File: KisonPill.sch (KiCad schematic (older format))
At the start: 39 parts, among them J1 USB_C_Receptacle_USB2.0, J2 Conn_01x19_Male, J3 Conn_01x19_Male, Q1 2N3904S-RTK/PS, Q2 2N3904S-RTK/PS, SW1 SW_Push, SW2 SW_Push, U1 CP2102N-A01-GQFN28, U2 ESP32-WROOM-32D, U3 SPX1117M3-L-3-3/TR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

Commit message: V2
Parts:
- U4: footprint KisonCommon:jtag1.27-12 -> KisonCommon:jtag1.27-10
- U7: footprint Connector_Molex:Molex_CLIK-Mate_502382-1270_1x12-1MP_P1.25mm_Vertical -> Connector_Molex:Molex_CLIK-Mate_502382-1070_1x10-1MP_P1.25mm_Vertical
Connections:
- net labels added: CP2102RX, CP2102TX, ESPRX, ESPTX
- net labels removed: RXD, RXD0, TXD, TXD0
- wire segments 56 -> 52
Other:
- moved on the sheet: R14, R15, R2, R3
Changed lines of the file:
@@
 P 1100 950
 F 0 "C1" H 1215 996 50  0000 L CNN
-F 1 "4.7uf/6.3v" H 1215 905 50  0000 L CNN
+F 1 "4.7uf/6.3v" H 650 850 50  0000 L CNN
 F 2 "Capacitor_SMD:C_0603_1608Metric" H 1138 800 50  0001 C CNN
 F 3 "~" H 1100 950 50  0001 C CNN
@@
 	1800 1200 1900 1200
 Connection ~ 1800 1200
-Text Label 1250 3000 0    50   ~ 0
-TXD0
-Text Label 1250 3150 0    50   ~ 0
-RXD0
-$Comp
-L Device:R R2
-U 1 1 6052F69F
-P 1000 3150
-F 0 "R2" V 1000 3150 50  0000 C CNN
-F 1 "0" V 884 3150 50  0000 C CNN
-F 2 "Resistor_SMD:R_0603_1608Metric" V 930 3150 50  0001 C CNN
-F 3 "~" H 1000 3150 50  0001 C CNN
-F 4 "C429667" H 1000 3150 50  0001 C CNN "LCSC"
-	1    1000 3150
-	0    -1   -1   0
-$EndComp
 $Comp
 L Device:R R3
 U 1 1 6052FB68
-P 1000 3000
-F 0 "R3" V 1000 3000 50  0000 C CNN
-F 1 "0" V 900 3000 50  0000 C CNN
-F 2 "Resistor_SMD:R_0603_1608Metric" V 930 3000 50  0001 C CNN
-F 3 "~" H 1000 3000 50  0001 C CNN
-F 4 "C429667" H 1000 3000 50  0001 C CNN "LCSC"
-	1    1000 3000
+P 1070 2990
+F 0 "R3" V 1070 2990 50  0000 C CNN
+F 1 "0" V 970 2990 50  0000 C CNN
+F 2 "Resistor_SMD:R_0603_1608Metric" V 1000 2990 50  0001 C CNN
+F 3 "~" H 1070 2990 50  0001 C CNN
+F 4 "C429667" H 1070 2990 50  0001 C CNN "LCSC"
+	1    1070 2990
 	0    1    1    0
 $EndComp
-Text Label 750  3150 2    50   ~ 0
-TXD
-Text Label 750  3000 2    50   ~ 0
-RXD
-Wire Wire Line
-	1250 3150 1150 3150
-Wire Wire Line
-	1250 3000 1150 3000
-Wire Wire Line
-	850  3150 750  3150
-Wire Wire Line
-	850  3000 750  3000
 $Comp
 L power:GND #PWR0107
@@
 	0    -1   -1   0
 $EndComp
-Text Label 2700 1700 0    50   ~ 0
-TXD
-Text Label 2700 1600 0    50   ~ 0
-RXD
 Wire Wire Line
 	2400 1600 2700 1600
@@
 Text Label 8050 1500 2    50   ~ 0
 EN
-Text Label 9250 1800 0    50   ~ 0
-RXD0
-Text Label 9250 1600 0    50   ~ 0
-TXD0
 Text Label 5760 910  0    50   ~ 0
 EN
-Text Label 5760 980  0    50   ~ 0
+Text Label 5760 1000 0    50   ~ 0
 IO12
-Text Label 5760 1050 0    50   ~ 0
-IO14
 $Comp
 L Regulator_Linear:AZ1117-3.3 U3
@@
 Text Label 6730 3810 0    50   ~ 0
 IO22
-Text Label 6730 3910 0    50   ~ 0
-TXD0
-Text Label 6730 4010 0    50   ~ 0
-RXD0
 Text Label 6730 4110 0    50   ~ 0
 IO21
@@
 $EndComp
 $Comp
-L power:+3V3 #PWR0124
-U 1 1 6059C21E
-P 6040 1120
-F 0 "#PWR0124" H 6040 970 50  0001 C CNN
-F 1 "+3V3" H 6055 1293 50  0000 C CNN
-F 2 "" H 6040 1120 50  0001 C CNN
-F 3 "" H 6040 1120 50  0001 C CNN
-	1    6040 1120
-	1    0    0    -1
-$EndComp
-Wire Wire Line
-	6040 1120 5760 1120
-$Comp
-L Device:R R15
-U 1 1 605D512D
-P 6320 1190
-F 0 "R15" V 6320 1190 50  0000 C CNN
-F 1 "0" V 6400 1190 50  0000 C CNN
-F 2 "Resistor_SMD:R_0603_1608Metric" V 6250 1190 50  0001 C CNN
-F 3 "~" H 6320 1190 50  0001 C CNN
-	1    6320 1190
-	0    1    1    0
-$EndComp
-Text Label 6470 1190 0    50   ~ 0
-TXD0
-$Comp
 L KisonCommon:ESP32FullConnector U7
 U 1 1 605F623D
@@
 F 0 "U7" H 5560 2304 50  0000 C CNN
 F 1 "ESP32FullConnector" H 5560 2213 50  0000 C CNN
-F 2 "Connector_Molex:Molex_CLIK-Mate_502382-1270_1x12-1MP_P1.25mm_Vertical" H 5750 1880 50  0001 C CNN
+F 2 "Connector_Molex:Molex_CLIK-Mate_502382-1070_1x10-1MP_P1.25mm_Vertical" H 5750 1880 50  0001 C CNN
 F 3 "" H 5750 1880 50  0001 C CNN
 	1    5750 1880
@@
 	-1   0    0    1
 $EndComp
-Text Label 5340 980  2    50   ~ 0
+Text Label 5340 1000 2    50   ~ 0
 IO13
-Text Label 5340 1050 2    50   ~ 0
+Text Label 5340 1090 2    50   ~ 0
 IO15
 Wire Wire Line
 	5120 910  5340 910
-Text Label 5340 1260 3    50   ~ 0
+Text Label 5340 1180 2    50   ~ 0
 IO0
-Text Label 4740 1190 2    50   ~ 0
-RXD0
 $Comp
 L KisonCommon:ESP32FullConnector U4
@@
 F 0 "U4" H 5550 1544 50  0000 C CNN
 F 1 "ESP32FullConnector-KisonCommon" H 5550 1453 50  0000 C CNN
-F 2 "KisonCommon:jtag1.27-12" H 5740 1120 50  0001 C CNN
+F 2 "KisonCommon:jtag1.27-10" H 5740 1120 50  0001 C CNN
 F 3 "" H 5740 1120 50  0001 C CNN
 	1    5740 1120
@@
 	-1   0    0    1
 $EndComp
-Text Label 5350 1740 2    50   ~ 0
+Text Label 5350 1760 2    50   ~ 0
 IO13
-Text Label 5350 1810 2    50   ~ 0
+Text Label 5350 1850 2    50   ~ 0
 IO15
 Wire Wire Line
 	5130 1670 5350 1670
-Text Label 5350 2020 3    50   ~ 0
+Text Label 5350 1940 2    50   ~ 0
 IO0
 Text Label 5770 1670 0    50   ~ 0
 EN
-Text Label 5770 1740 0    50   ~ 0
+Text Label 5770 1760 0    50   ~ 0
 IO12
-Text Label 5770 1810 0    50   ~ 0
+Text Label 5770 1850 0    50   ~ 0
 IO14
 $Comp
 L power:+3V3 #PWR010
 U 1 1 6061353C
-P 6050 1880
-F 0 "#PWR010" H 6050 1730 50  0001 C CNN
-F 1 "+3V3" H 6065 2053 50  0000 C CNN
-F 2 "" H 6050 1880 50  0001 C CNN
-F 3 "" H 6050 1880 50  0001 C CNN
-	1    6050 1880
-	1    0    0    -1
-$EndComp
-Wire Wire Line
-	6050 1880 5770 1880
-Wire Wire Line
-	5770 1950 6170 1950
-Wire Wire Line
-	6170 1950 6170 1190
+P 6050 1940
+F 0 "#PWR010" H 6050 1790 50  0001 C CNN
+F 1 "+3V3" H 6065 2113 50  0000 C CNN
+F 2 "" H 6050 1940 50  0001 C CNN
+F 3 "" H 6050 1940 50  0001 C CNN
+	1    6050 1940
+	1    0    0    -1
+$EndComp
+Wire Wire Line
+	6050 1940 5770 1940
+Wire Wire Line
+	5770 2030 6170 2030
 Text Notes 4400 610  0    50   ~ 0
 Should we isolate IO0 and rx,tx from Connector to on board?
-$Comp
-L Device:R R14
-U 1 1 605CA1B8
-P 4890 1190
-F 0 "R14" V 4890 1190 50  0000 C CNN
-F 1 "0" V 4970 1190 50  0000 C CNN
-F 2 "Resistor_SMD:R_0603_1608Metric" V 4820 1190 50  0001 C CNN
-F 3 "~" H 4890 1190 50  0001 C CNN
-	1    4890 1190
-	0    1    1    0
-$EndComp
-Wire Wire Line
-	5040 1190 5340 1190
-Connection ~ 6170 1190
-Wire Wire Line
-	5760 1190 6170 1190
-Connection ~ 5040 1190
-Wire Wire Line
-	5040 1950 5040 1190
-Wire Wire Line
-	5350 1950 5040 1950
+Wire Wire Line
+	5350 2030 5040 2030
 $Comp
 L Connector:Conn_01x19_Male J3
@@
 	0    1    1    0
 $EndComp
+Wire Wire Line
+	5340 1270 5040 1270
+Connection ~ 5040 1270
+Wire Wire Line
+	5040 1270 5040 2030
+$Comp
+L Device:R R14
+U 1 1 605CA1B8
+P 4890 1270
+F 0 "R14" V 4890 1270 50  0000 C CNN
+F 1 "0" V 4970 1270 50  0000 C CNN
+F 2 "Resistor_SMD:R_0603_1608Metric" V 4820 1270 50  0001 C CNN
+F 3 "~" H 4890 1270 50  0001 C CNN
+	1    4890 1270
+	0    1    1    0
+$EndComp
+Wire Wire Line
+	5760 1270 6170 1270
+Wire Wire Line
+	6170 1270 6170 2030
+$Comp
+L Device:R R15
+U 1 1 605D512D
+P 6320 1270
+F 0 "R15" V 6320 1270 50  0000 C CNN
+F 1 "0" V 6400 1270 50  0000 C CNN
+F 2 "Resistor_SMD:R_0603_1608Metric" V 6250 1270 50  0001 C CNN
+F 3 "~" H 6320 1270 50  0001 C CNN
+	1    6320 1270
+	0    1    1    0
+$EndComp
+Connection ~ 6170 1270
+Wire Wire Line
+	6040 1180 5760 1180
+$Comp
+L power:+3V3 #PWR0124
+U 1 1 6059C21E
+P 6040 1180
+F 0 "#PWR0124" H 6040 1030 50  0001 C CNN
+F 1 "+3V3" H 6055 1353 50  0000 C CNN
+F 2 "" H 6040 1180 50  0001 C CNN
+F 3 "" H 6040 1180 50  0001 C CNN
+	1    6040 1180
+	1    0    0    -1
+$EndComp
+Text Label 5760 1090 0    50   ~ 0
+IO14
+Text Label 4740 1270 2    50   ~ 0
+ESPRX
+Text Label 1220 3130 0    50   ~ 0
+ESPRX
+Text Label 9250 1800 0    50   ~ 0
+ESPRX
+Text Label 9250 1600 0    50   ~ 0
+ESPTX
+Text Label 6470 1270 0    50   ~ 0
+ESPTX
+Text Label 1220 2990 0    50   ~ 0
+ESPTX
+Text Label 920  2990 2    50   ~ 0
+CP2102RX
+$Comp
+L Device:R R2
+U 1 1 6052F69F
+P 1070 3130
+F 0 "R2" V 1070 3130 50  0000 C CNN
+F 1 "0" V 954 3130 50  0000 C CNN
+F 2 "Resistor_SMD:R_0603_1608Metric" V 1000 3130 50  0001 C CNN
+F 3 "~" H 1070 3130 50  0001 C CNN
+F 4 "C429667" H 1070 3130 50  0001 C CNN "LCSC"
+	1    1070 3130
+	0    -1   -1   0
+$EndComp
+Text Label 920  3130 2    50   ~ 0
+CP2102TX
+Text Label 2700 1700 0    50   ~ 0
+CP2102TX
+Text Label 2700 1600 0    50   ~ 0
+CP2102RX
+Text Label 6730 3910 0    50   ~ 0
+ESPTX
+Text Label 6730 4010 0    50   ~ 0
+ESPRX
 $EndSCHEMATC

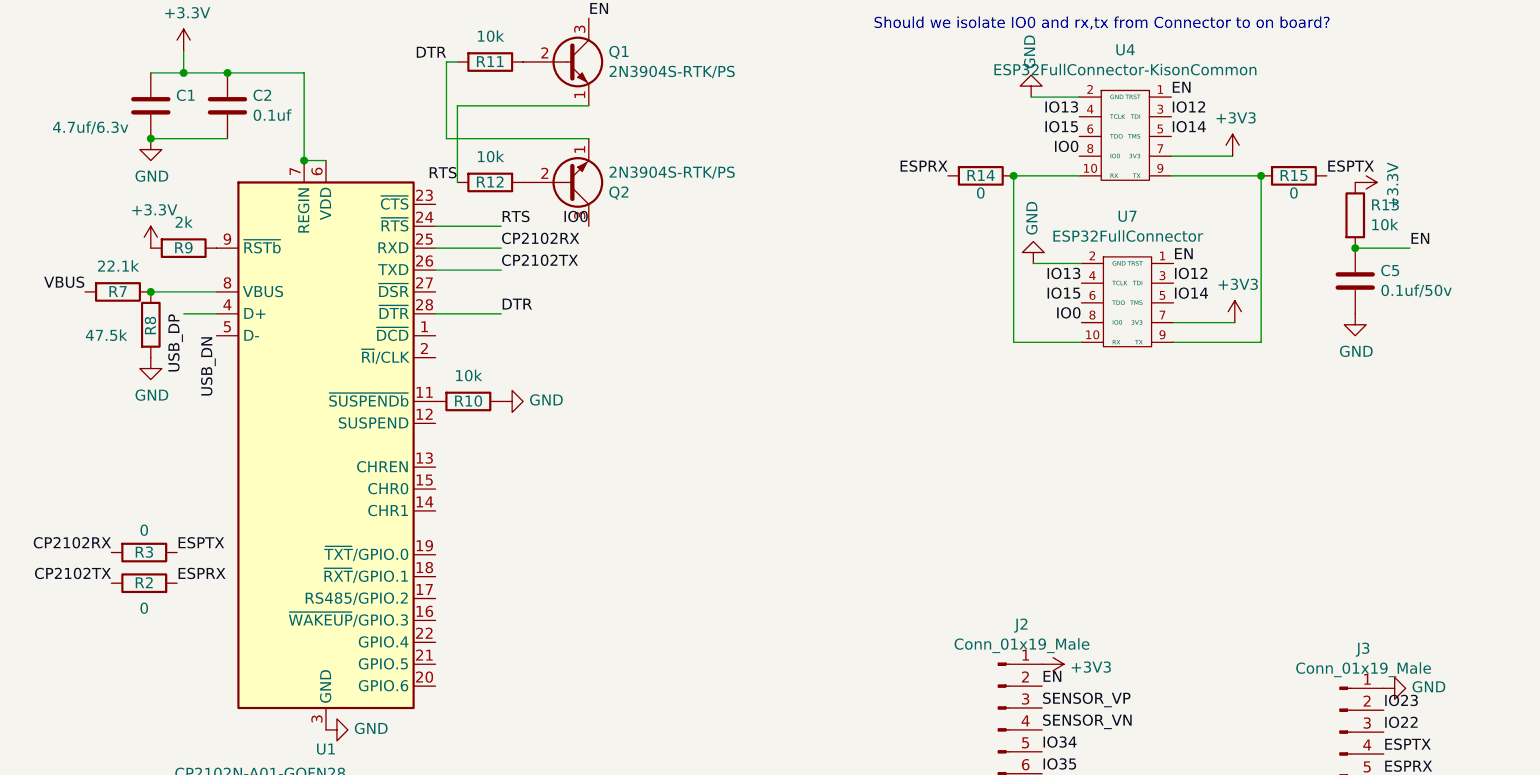
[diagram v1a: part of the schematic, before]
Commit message: Added a switch to pick TX
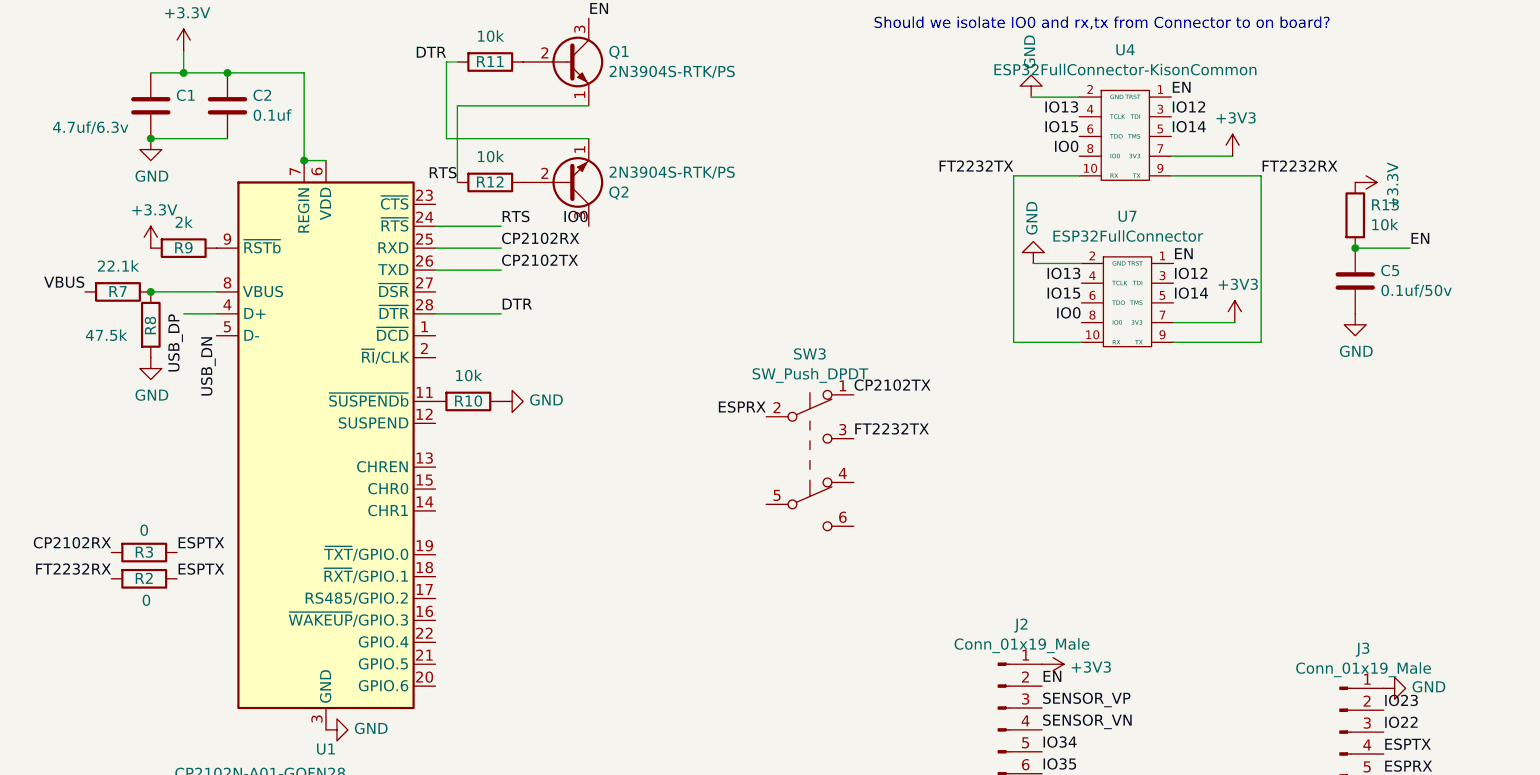
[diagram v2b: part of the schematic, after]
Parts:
- removed R14, R15: 0, Resistor_SMD:R_0603_1608Metric, symbol Device:R
- added SW3: SW_Push_DPDT, KisonCommon:MSS22D18G2, symbol Switch:SW_Push_DPDT
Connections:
- net CP2102TX: now also SW3.1 (A); no longer R2.1
- net ESPRX: now also SW3.2 (B); no longer R2.2
- net ESPTX: now also R2.1
- net FT2232TX: now reaches U4.10 (RX), U7.10 (RX)
- net FT2232TX: now also SW3.3 (C)
- net FT2232RX: now reaches U4.9 (TX), U7.9 (TX)
- net FT2232RX: now also R2.2
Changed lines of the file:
@@
 Connection ~ 1800 1200
-$Comp
-L Device:R R3
-U 1 1 6052FB68
-P 1070 2990
-F 0 "R3" V 1070 2990 50  0000 C CNN
-F 1 "0" V 970 2990 50  0000 C CNN
-F 2 "Resistor_SMD:R_0603_1608Metric" V 1000 2990 50  0001 C CNN
-F 3 "~" H 1070 2990 50  0001 C CNN
-F 4 "C429667" H 1070 2990 50  0001 C CNN "LCSC"
-	1    1070 2990
-	0    1    1    0
-$EndComp
 $Comp
 L power:GND #PWR0107
@@
 Wire Wire Line
 	5340 1270 5040 1270
-Connection ~ 5040 1270
 Wire Wire Line
 	5040 1270 5040 2030
-$Comp
-L Device:R R14
-U 1 1 605CA1B8
-P 4890 1270
-F 0 "R14" V 4890 1270 50  0000 C CNN
-F 1 "0" V 4970 1270 50  0000 C CNN
-F 2 "Resistor_SMD:R_0603_1608Metric" V 4820 1270 50  0001 C CNN
-F 3 "~" H 4890 1270 50  0001 C CNN
-	1    4890 1270
-	0    1    1    0
-$EndComp
 Wire Wire Line
 	5760 1270 6170 1270
 Wire Wire Line
 	6170 1270 6170 2030
-$Comp
-L Device:R R15
-U 1 1 605D512D
-P 6320 1270
-F 0 "R15" V 6320 1270 50  0000 C CNN
-F 1 "0" V 6400 1270 50  0000 C CNN
-F 2 "Resistor_SMD:R_0603_1608Metric" V 6250 1270 50  0001 C CNN
-F 3 "~" H 6320 1270 50  0001 C CNN
-	1    6320 1270
-	0    1    1    0
-$EndComp
-Connection ~ 6170 1270
 Wire Wire Line
 	6040 1180 5760 1180
@@
 Text Label 5760 1090 0    50   ~ 0
 IO14
-Text Label 4740 1270 2    50   ~ 0
-ESPRX
-Text Label 1220 3130 0    50   ~ 0
-ESPRX
 Text Label 9250 1800 0    50   ~ 0
 ESPRX
 Text Label 9250 1600 0    50   ~ 0
-ESPTX
-Text Label 6470 1270 0    50   ~ 0
 ESPTX
 Text Label 1220 2990 0    50   ~ 0
@@
 Text Label 920  2990 2    50   ~ 0
 CP2102RX
-$Comp
-L Device:R R2
-U 1 1 6052F69F
-P 1070 3130
-F 0 "R2" V 1070 3130 50  0000 C CNN
-F 1 "0" V 954 3130 50  0000 C CNN
-F 2 "Resistor_SMD:R_0603_1608Metric" V 1000 3130 50  0001 C CNN
-F 3 "~" H 1070 3130 50  0001 C CNN
-F 4 "C429667" H 1070 3130 50  0001 C CNN "LCSC"
-	1    1070 3130
-	0    -1   -1   0
-$EndComp
-Text Label 920  3130 2    50   ~ 0
-CP2102TX
 Text Label 2700 1700 0    50   ~ 0
 CP2102TX
@@
 Text Label 6730 4010 0    50   ~ 0
 ESPRX
+Text Label 5040 1270 2    50   ~ 0
+FT2232TX
+Text Label 6170 1270 0    50   ~ 0
+FT2232RX
+$Comp
+L Switch:SW_Push_DPDT SW3
+U 1 1 6083AE64
+P 4110 2570
+F 0 "SW3" H 4110 3055 50  0000 C CNN
+F 1 "SW_Push_DPDT" H 4110 2964 50  0000 C CNN
+F 2 "KisonCommon:MSS22D18G2" H 4110 2770 50  0001 C CNN
+F 3 "~" H 4110 2770 50  0001 C CNN
+	1    4110 2570
+	1    0    0    -1
+$EndComp
+Text Label 3910 2370 2    50   ~ 0
+ESPRX
+Text Label 4310 2270 0    50   ~ 0
+CP2102TX
+Text Label 4310 2470 0    50   ~ 0
+FT2232TX
+Text Label 920  3110 2    50   ~ 0
+FT2232RX
+$Comp
+L Device:R R2
+U 1 1 6084D46E
+P 1070 3110
+F 0 "R2" V 1070 3110 50  0000 C CNN
+F 1 "0" V 1170 3120 50  0000 C CNN
+F 2 "Resistor_SMD:R_0603_1608Metric" V 1000 3110 50  0001 C CNN
+F 3 "~" H 1070 3110 50  0001 C CNN
+F 4 "C429667" H 1070 3110 50  0001 C CNN "LCSC"
+	1    1070 3110
+	0    1    1    0
+$EndComp
+$Comp
+L Device:R R3
+U 1 1 6052FB68
+P 1070 2990
+F 0 "R3" V 1070 2990 50  0000 C CNN
+F 1 "0" V 970 2990 50  0000 C CNN
+F 2 "Resistor_SMD:R_0603_1608Metric" V 1000 2990 50  0001 C CNN
+F 3 "~" H 1070 2990 50  0001 C CNN
+F 4 "C429667" H 1070 2990 50  0001 C CNN "LCSC"
+	1    1070 2990
+	0    1    1    0
+$EndComp
+Text Label 1220 3110 0    50   ~ 0
+ESPTX
 $EndSCHEMATC

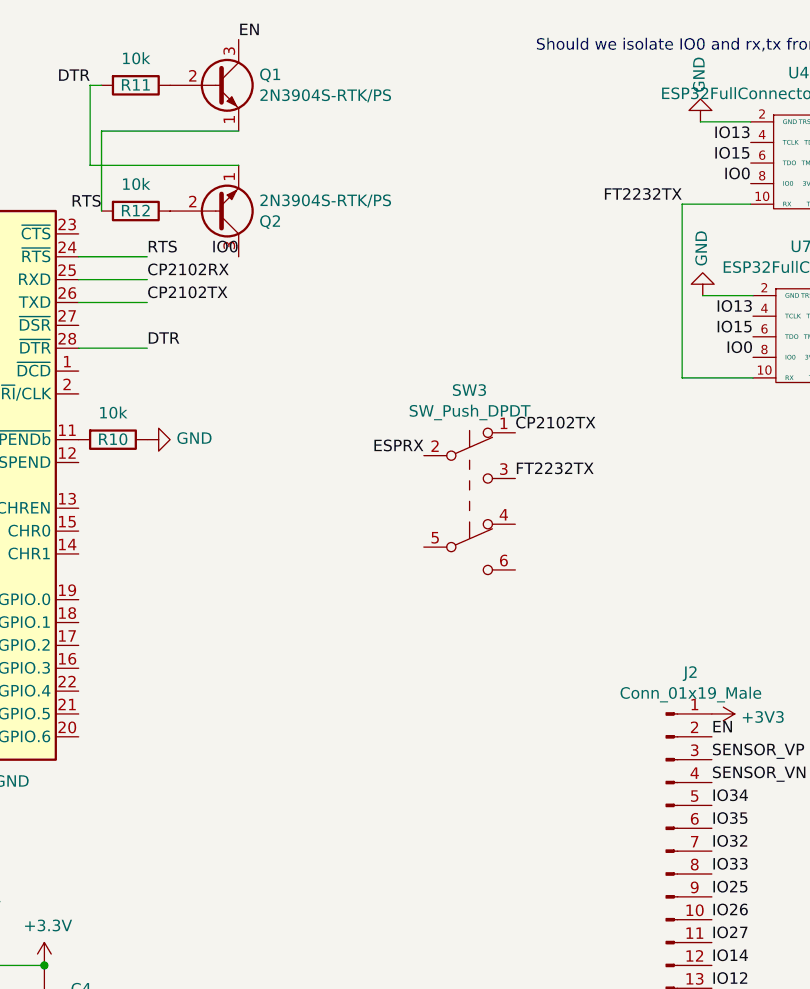
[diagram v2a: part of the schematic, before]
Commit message: Modify Button
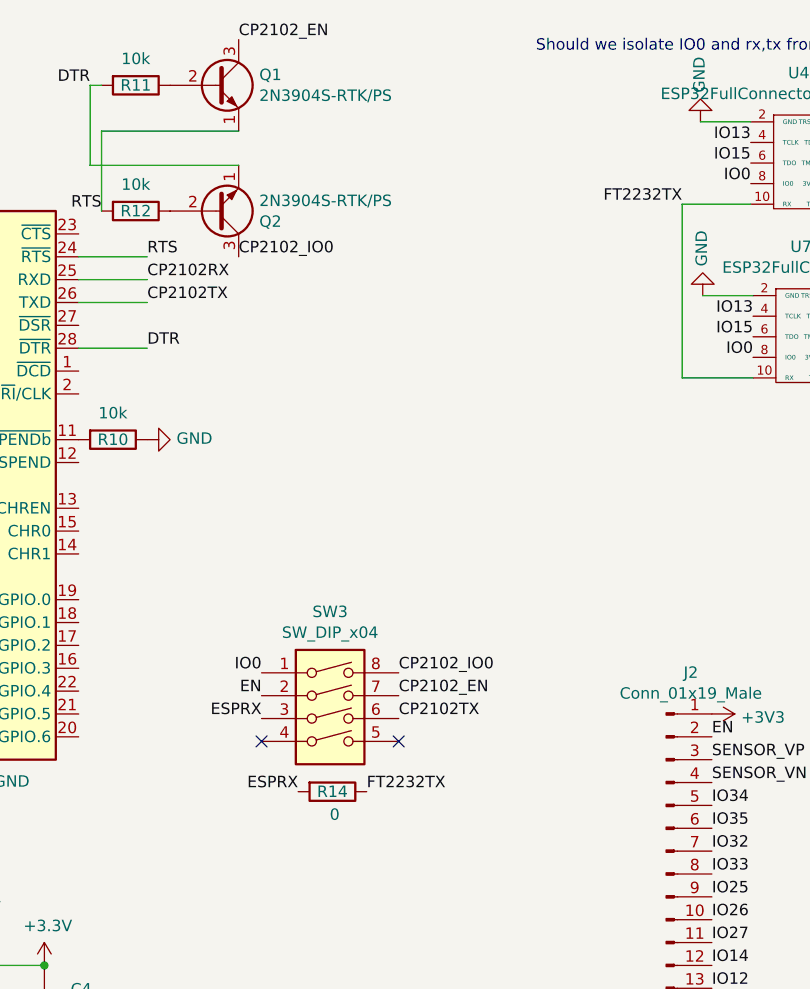
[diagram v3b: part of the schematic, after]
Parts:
- removed SW3: SW_Push_DPDT, KisonCommon:MSS22D18G2, symbol Switch:SW_Push_DPDT
- added R14: 0, Resistor_SMD:R_0603_1608Metric, symbol Device:R
- added SW3: SW_DIP_x04, Button_Switch_SMD:SW_DIP_SPSTx04_Slide_Copal_CHS-04B_W7.62mm_P1.27mm, symbol Switch:SW_DIP_x04
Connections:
- net CP2102TX: now also SW3.6
- net EN: now also SW3.2; no longer Q1.3 (C)
- net ESPRX: now also R14.2, SW3.3
- net FT2232TX: now also R14.1
- net IO0: now also SW3.1; no longer Q2.3 (C)
- new net CP2102_EN: Q1.3 (C), SW3.7
- new net CP2102_IO0: Q2.3 (C), SW3.8
- no-connect marks 0 -> 2
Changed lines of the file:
@@
 Wire Wire Line
 	2450 1100 3100 1100
-Text Label 3100 1500 2    50   ~ 0
-IO0
-Text Label 3100 550  0    50   ~ 0
-EN
 $Comp
 L power:+3.3V #PWR012
@@
 Wire Wire Line
 	5120 910  5340 910
-Text Label 5340 1180 2    50   ~ 0
-IO0
 $Comp
 L KisonCommon:ESP32FullConnector U4
@@
 Wire Wire Line
 	5130 1670 5350 1670
-Text Label 5350 1940 2    50   ~ 0
-IO0
 Text Label 5770 1670 0    50   ~ 0
 EN
@@
 Text Label 6170 1270 0    50   ~ 0
 FT2232RX
-$Comp
-L Switch:SW_Push_DPDT SW3
-U 1 1 6083AE64
-P 4110 2570
-F 0 "SW3" H 4110 3055 50  0000 C CNN
-F 1 "SW_Push_DPDT" H 4110 2964 50  0000 C CNN
-F 2 "KisonCommon:MSS22D18G2" H 4110 2770 50  0001 C CNN
-F 3 "~" H 4110 2770 50  0001 C CNN
-	1    4110 2570
-	1    0    0    -1
-$EndComp
-Text Label 3910 2370 2    50   ~ 0
+Text Label 3360 3840 2    50   ~ 0
 ESPRX
-Text Label 4310 2270 0    50   ~ 0
-CP2102TX
-Text Label 4310 2470 0    50   ~ 0
+Text Label 3660 3840 0    50   ~ 0
 FT2232TX
 Text Label 920  3110 2    50   ~ 0
@@
 Text Label 1220 3110 0    50   ~ 0
 ESPTX
+$Comp
+L Switch:SW_DIP_x04 SW3
+U 1 1 609A3C08
+P 3500 3520
+F 0 "SW3" H 3500 3987 50  0000 C CNN
+F 1 "SW_DIP_x04" H 3500 3896 50  0000 C CNN
+F 2 "Button_Switch_SMD:SW_DIP_SPSTx04_Slide_Copal_CHS-04B_W7.62mm_P1.27mm" H 3500 3520 50  0001 C CNN
+F 3 "~" H 3500 3520 50  0001 C CNN
+	1    3500 3520
+	1    0    0    -1
+$EndComp
+NoConn ~ 3800 3620
+NoConn ~ 3200 3620
+Text Label 5350 1940 2    50   ~ 0
+IO0
+Text Label 5340 1180 2    50   ~ 0
+IO0
+Text Label 3100 550  0    50   ~ 0
+CP2102_EN
+Text Label 3100 1500 0    50   ~ 0
+CP2102_IO0
+Text Label 3800 3320 0    50   ~ 0
+CP2102_IO0
+Text Label 3200 3320 2    50   ~ 0
+IO0
+Text Label 3800 3420 0    50   ~ 0
+CP2102_EN
+Text Label 3200 3420 2    50   ~ 0
+EN
+Text Label 3200 3520 2    50   ~ 0
+ESPRX
+Text Label 3800 3520 0    50   ~ 0
+CP2102TX
+$Comp
+L Device:R R14
+U 1 1 608CD0E9
+P 3510 3840
+F 0 "R14" V 3510 3840 50  0000 C CNN
+F 1 "0" V 3610 3850 50  0000 C CNN
+F 2 "Resistor_SMD:R_0603_1608Metric" V 3440 3840 50  0001 C CNN
+F 3 "~" H 3510 3840 50  0001 C CNN
+F 4 "C429667" H 3510 3840 50  0001 C CNN "LCSC"
+	1    3510 3840
+	0    1    1    0
+$EndComp
 $EndSCHEMATC
